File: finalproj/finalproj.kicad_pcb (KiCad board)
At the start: 2 copper layers, 83 parts, among them J1 Conn_01x01, J10 MotorA Out, J11 MotorB Out, J2 Conn_01x01, J3 Conn_01x01, J4 Programmer_Conn, J5 Stepper_Motor_Controller, J6 Conn_01x01, J7 LIDAR_Connector, J9 RPI_UART_Conn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

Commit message: jlcboard2 ready for review
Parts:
- moved POW1 99.9 mm to (15.6, 15.4), turned to 90 degrees
- moved POW3 43.8 mm to (108.9, 56.1)
- moved H1 25.2 mm to (12.4, 42.6)
- moved C25 21.6 mm to (62.2, 12.6), turned to 0 degrees
- moved C20 13.2 mm to (69.4, 81.2)
- moved C2 8.26 mm to (92.8, 30.2), turned to 90 degrees
- moved C1 4.24 mm to (97.0, 30.2), turned to 90 degrees
- moved G*** 2.62 mm to (90.0, 92.8)
- moved J1 1.58 mm to (45.2, 36.4)
- moved D1 1.34 mm to (91.0, 62.1), turned to 90 degrees
- moved J6 0.66 mm to (14.8, 28.4)
- moved D2 0.40 mm to (91.2, 57.9), turned to 90 degrees
- moved H2 0.21 mm to (108.4, 13.8)
- turned C14 to -90 degrees
- turned C15 to -90 degrees
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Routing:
- net EXT_5: track 115.1 -> 357.2 mm, vias 0 -> 4
- net EXT_12: track 35.1 -> 216.4 mm, vias 0 -> 10
- net EncoderBFeedback1: track 0.00 -> 112.4 mm, vias 0 -> 2
- net EncoderBFeedback2: track 0.00 -> 112.2 mm, vias 0 -> 2
- net EncoderAFeedback2: track 0.00 -> 81.5 mm, vias 0 -> 2
- net EncoderAFeedback1: track 0.00 -> 79.3 mm, vias 0 -> 2
- net MotorBPWM: track 0.00 -> 65.8 mm, vias 0 -> 2
- net STEP_PWM: track 0.00 -> 63.3 mm, vias 0 -> 2
- net MotorAIn1: track 0.00 -> 56.5 mm, vias 0 -> 6
- net MotorAIn2: track 0.00 -> 52.7 mm, vias 0 -> 3
- net MotorOutB1: track 19.0 -> 70.7 mm, vias 2 -> 3
- net STEP_DIR: track 0.00 -> 51.4 mm, vias 0 -> 2
- net MotorAPWM: track 0.00 -> 48.7 mm, vias 0 -> 4
- net MotorBIn1: track 0.00 -> 43.1 mm, vias 0 -> 2
- net MotorBIn2: track 0.00 -> 40.6 mm, vias 0 -> 2
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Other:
- board outline added: 105.4 x 104.4 mm

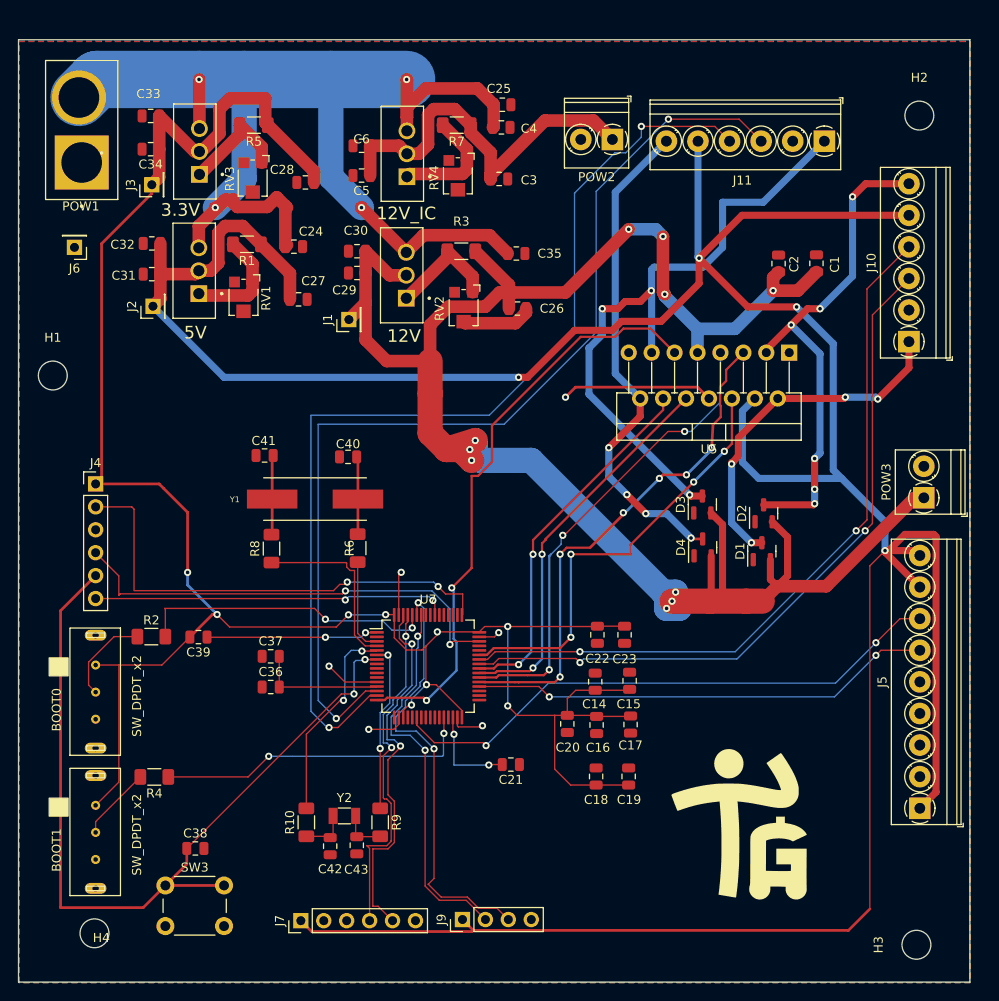
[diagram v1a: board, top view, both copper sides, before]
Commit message: got rid of all warnings and errors, board is 100x100mm
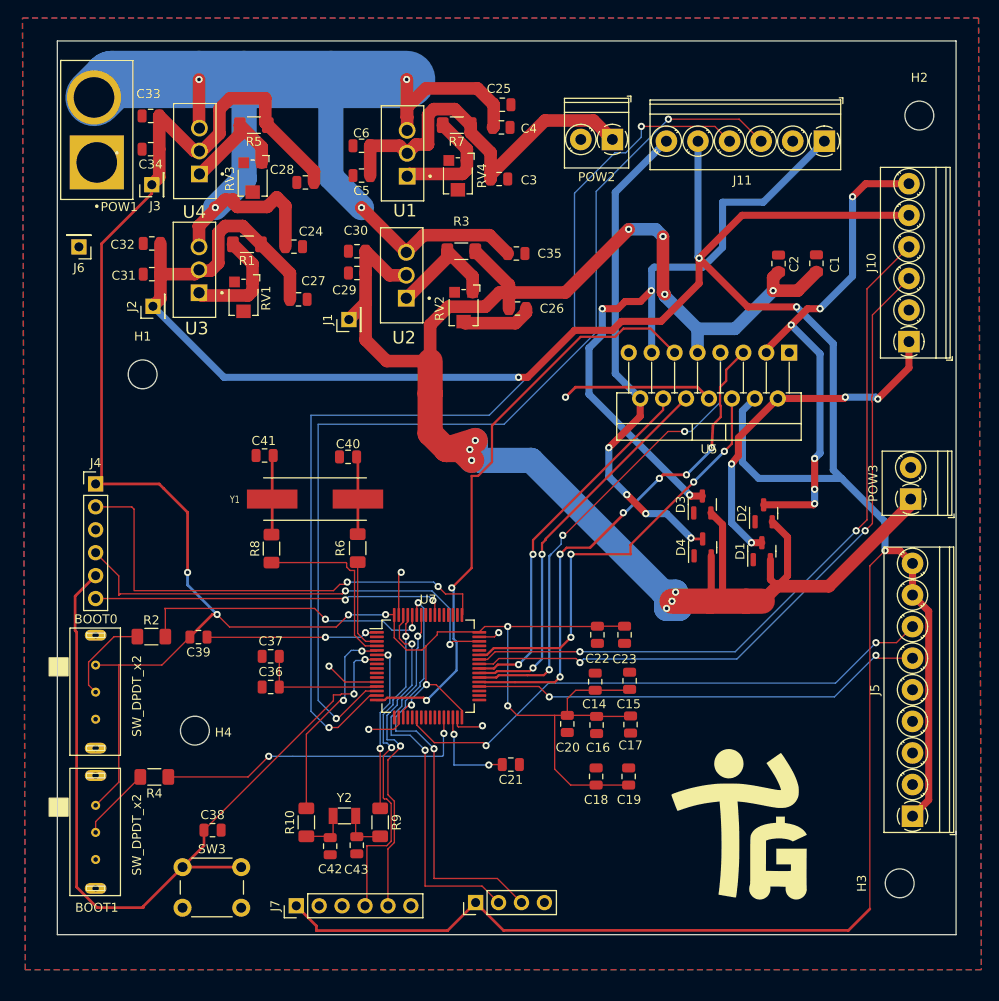
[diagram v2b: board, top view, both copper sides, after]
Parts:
- removed 12V, 12V_IC: LM1085-12, LM1085IT-5.0:TO254P1054X470X1955-3
- removed 3.3V: LM1085-3.3, LM1085IT-5.0:TO254P1054X470X1955-3
- removed 5V: LM1085-5.0, LM1085IT-5.0:TO254P1054X470X1955-3
- added U1: LM1085-12, LM1085IT-5.0:TO254P1054X470X1955-3, F.Cu at (51.7, 18.0)
- added U2: LM1085-12, LM1085IT-5.0:TO254P1054X470X1955-3, F.Cu at (51.6, 31.5)
- added U3: LM1085-5.0, LM1085IT-5.0:TO254P1054X470X1955-3, F.Cu at (28.6, 30.9)
- added U4: LM1085-3.3, LM1085IT-5.0:TO254P1054X470X1955-3, F.Cu at (28.6, 17.7)
- moved H4 25.1 mm to (28.1, 81.9)
- moved H1 9.95 mm to (22.4, 42.5)
- moved H3 7.06 mm to (106.2, 98.9)
- moved SW3 2.78 mm to (26.8, 97.1)
- moved C38 2.78 mm to (30.1, 93.0)
- moved J9 2.38 mm to (59.2, 101.0)
- moved J7 1.73 mm to (39.4, 101.3)
- moved POW1 1.67 mm to (17.3, 15.4)
- moved POW3 1.46 mm to (107.4, 56.3)
- moved J5 1.19 mm to (107.6, 91.4)
- moved J6 0.49 mm to (15.3, 28.3)
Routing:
- net EXT_5: track 357.2 -> 345.6 mm
- net LIDAR_SDA: track 41.4 -> 36.8 mm
- net NRST: track 94.4 -> 91.1 mm
- net BATTERY_VIN: track 134.0 -> 131.6 mm
- net EXT_12: track 216.4 -> 214.3 mm
- net LIDAR_SCL: track 39.0 -> 37.3 mm
- net STEP_PWM: track 63.3 -> 62.2 mm
- net STEP_DIR: track 51.4 -> 50.5 mm
- net RPI_UART_TX: track 42.4 -> 43.1 mm
- net RPI_UART_RX: track 48.0 -> 47.4 mm
- net MotorAIn1: track 56.5 -> 55.9 mm
- net EXT_3.3: track 242.0 -> 241.8 mm, vias 9 -> 8
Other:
- board size 105.4 x 104.4 mm -> 99.6 x 99 mm
